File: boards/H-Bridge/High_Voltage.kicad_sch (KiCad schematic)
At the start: 3 parts, among them IC2 MIC4606-1YML-TR, IC3 AD8410AWBRZ-RL

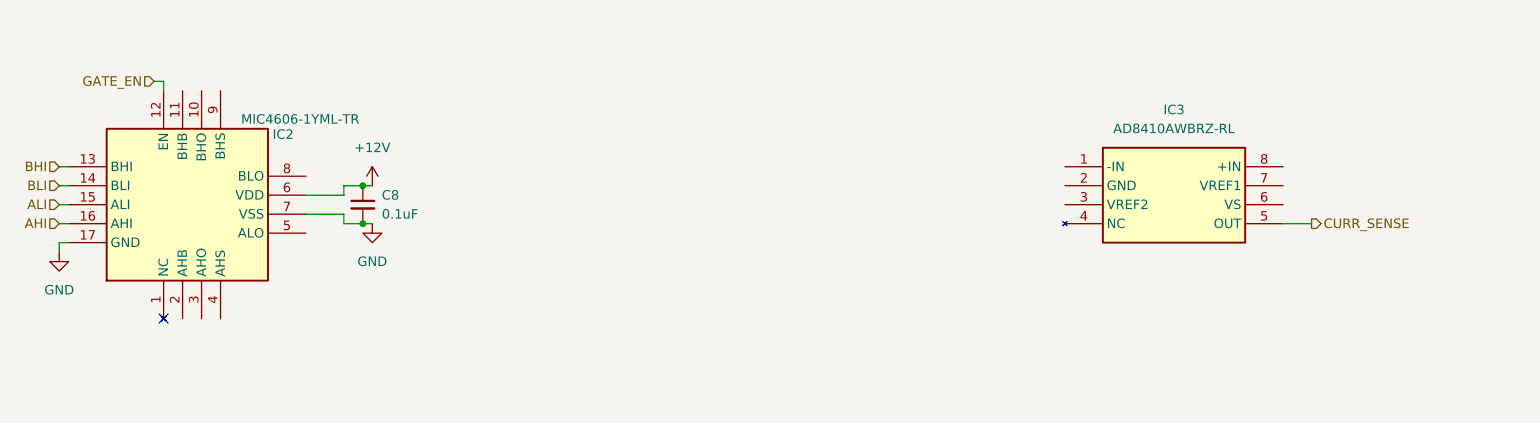
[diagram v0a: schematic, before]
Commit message: Added symbols + fixed sheet layout, low voltage nearly complete
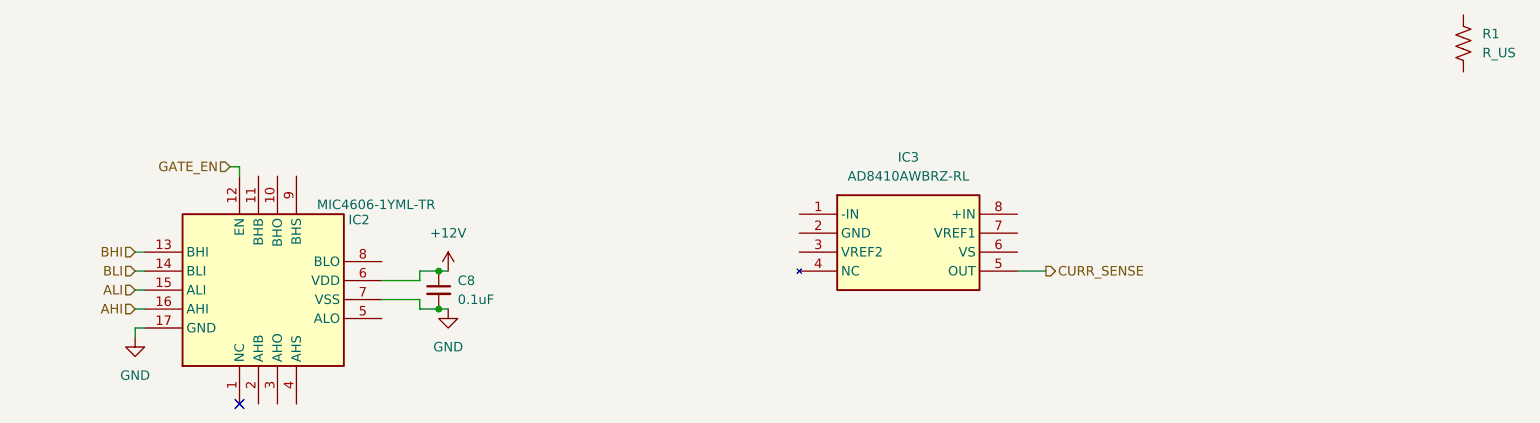
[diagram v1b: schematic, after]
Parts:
- added R1: R_US, symbol Device:R_US
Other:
- moved on the sheet: C8, IC2, IC3

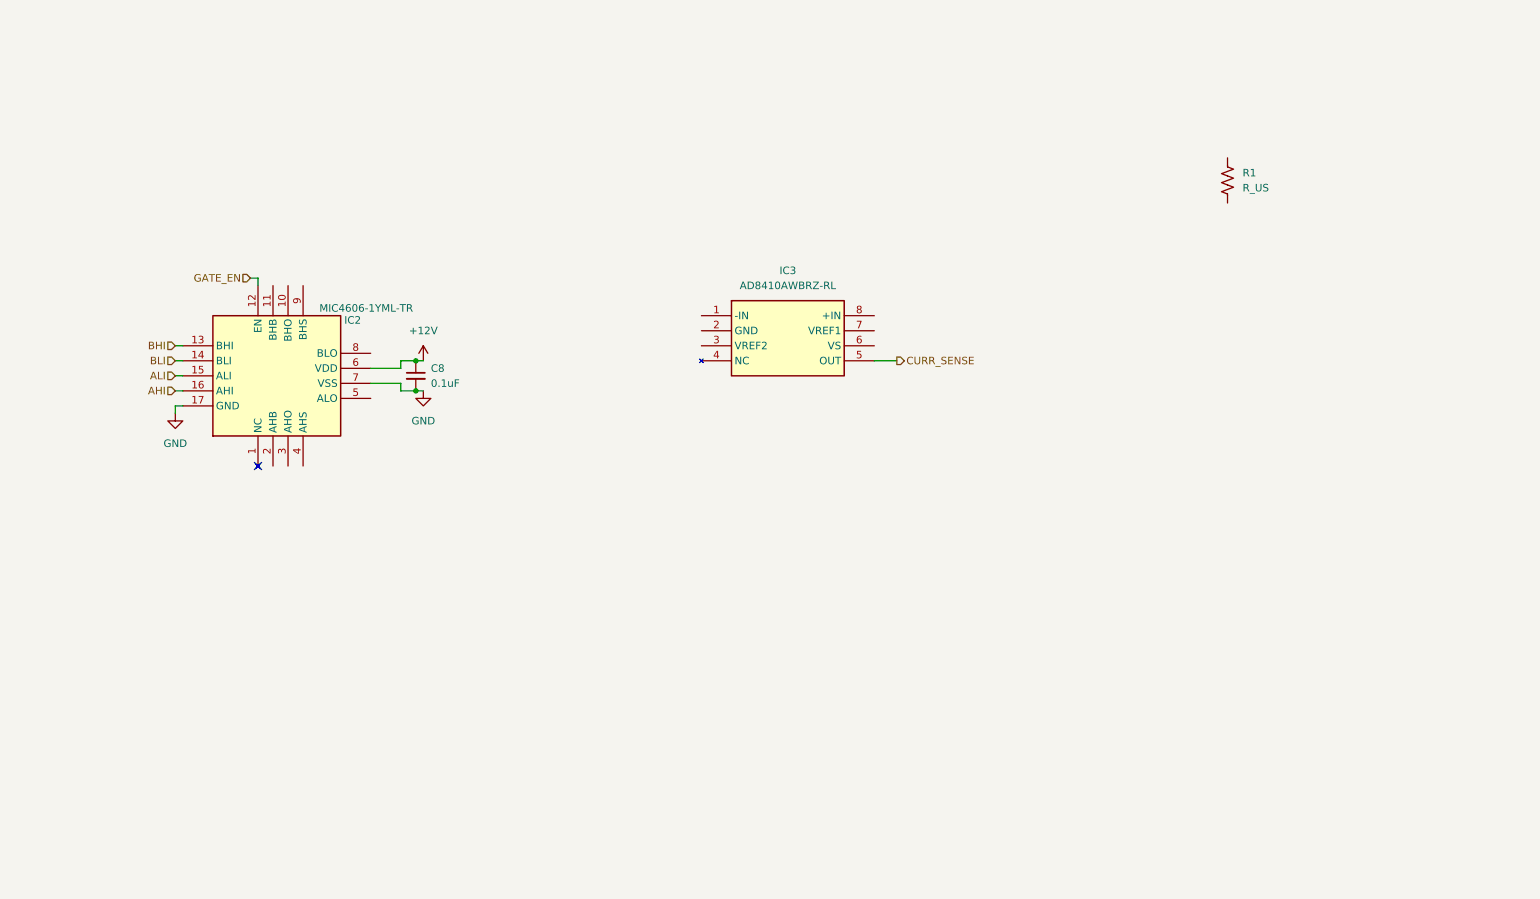
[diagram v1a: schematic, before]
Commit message: added fet sym,  hv schematic changes
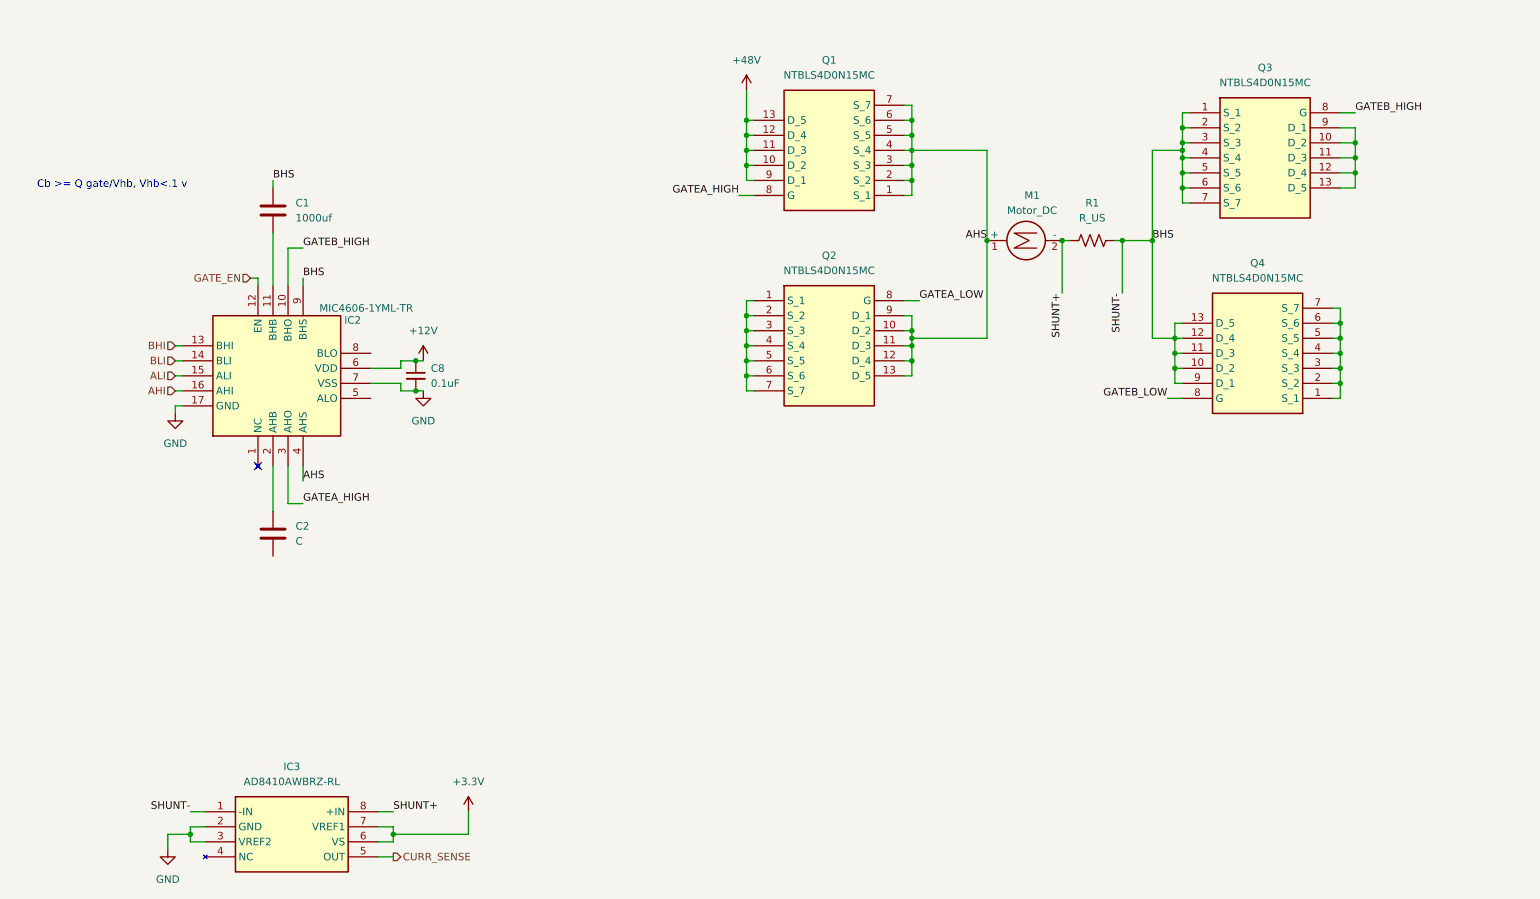
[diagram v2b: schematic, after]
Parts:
- added C1: 1000uf, symbol Device:C
- added C2: C, symbol Device:C
- added M1: Motor_DC, symbol Motor:Motor_DC
- added Q1, Q2, Q3, Q4: NTBLS4D0N15MC, High Power MOSFETs:NTBLS4D0N15MC, symbol High Power MOSFETs:NTBLS4D0N15MC
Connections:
- net GND: now also IC3.2 (GND), IC3.3 (VREF2)
- net BHS: now reaches IC3.1 (-IN)
- net BHS: now also IC2.9 (BHS), R1.2, C1.1, Q3.1 (S_1), Q3.2 (S_2), Q3.3 (S_3), Q3.4 (S_4), Q3.5 (S_5), Q3.6 (S_6), Q3.7 (S_7), Q4.10 (D_2), Q4.11 (D_3), Q4.12 (D_4), Q4.13 (D_5), Q4.9 (D_1)
- net +3.3V: now reaches IC3.6 (VS)
- net +3.3V: now also IC3.7 (VREF1)
- net SHUNT+: now reaches IC3.8 (+IN)
- net SHUNT+: now also R1.1, M1.2 (-)
- net GATEB_HIGH: now reaches IC2.10 (BHO)
- net GATEB_HIGH: now also Q3.8 (G)
- net at IC2.11 (BHB): now also C1.2
- net at IC2.2 (AHB): now also C2.1
- net GATEA_HIGH: now reaches IC2.3 (AHO)
- net GATEA_HIGH: now also Q1.8 (G)
- net AHS: now reaches IC2.4 (AHS)
- net AHS: now also M1.1 (+), Q1.1 (S_1), Q1.2 (S_2), Q1.3 (S_3), Q1.4 (S_4), Q1.5 (S_5), Q1.6 (S_6), Q1.7 (S_7), Q2.10 (D_2), Q2.11 (D_3), Q2.12 (D_4), Q2.13 (D_5), Q2.9 (D_1)
- new net: Q2.1 (S_1), Q2.2 (S_2), Q2.3 (S_3), Q2.4 (S_4), Q2.5 (S_5), Q2.6 (S_6), Q2.7 (S_7)
- new net: Q4.1 (S_1), Q4.2 (S_2), Q4.3 (S_3), Q4.4 (S_4), Q4.5 (S_5), Q4.6 (S_6), Q4.7 (S_7)
- new net: Q3.10 (D_2), Q3.11 (D_3), Q3.12 (D_4), Q3.13 (D_5), Q3.9 (D_1)
- new net +48V: Q1.10 (D_2), Q1.11 (D_3), Q1.12 (D_4), Q1.13 (D_5), Q1.9 (D_1)
- new net GATEA_LOW: Q2.8 (G)
- new net GATEB_LOW: Q4.8 (G)
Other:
- note added: "Cb >= Q gate/Vhb, Vhb<.1 v"
- moved on the sheet: IC3, R1

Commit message: finished schematic (i think), added footprints
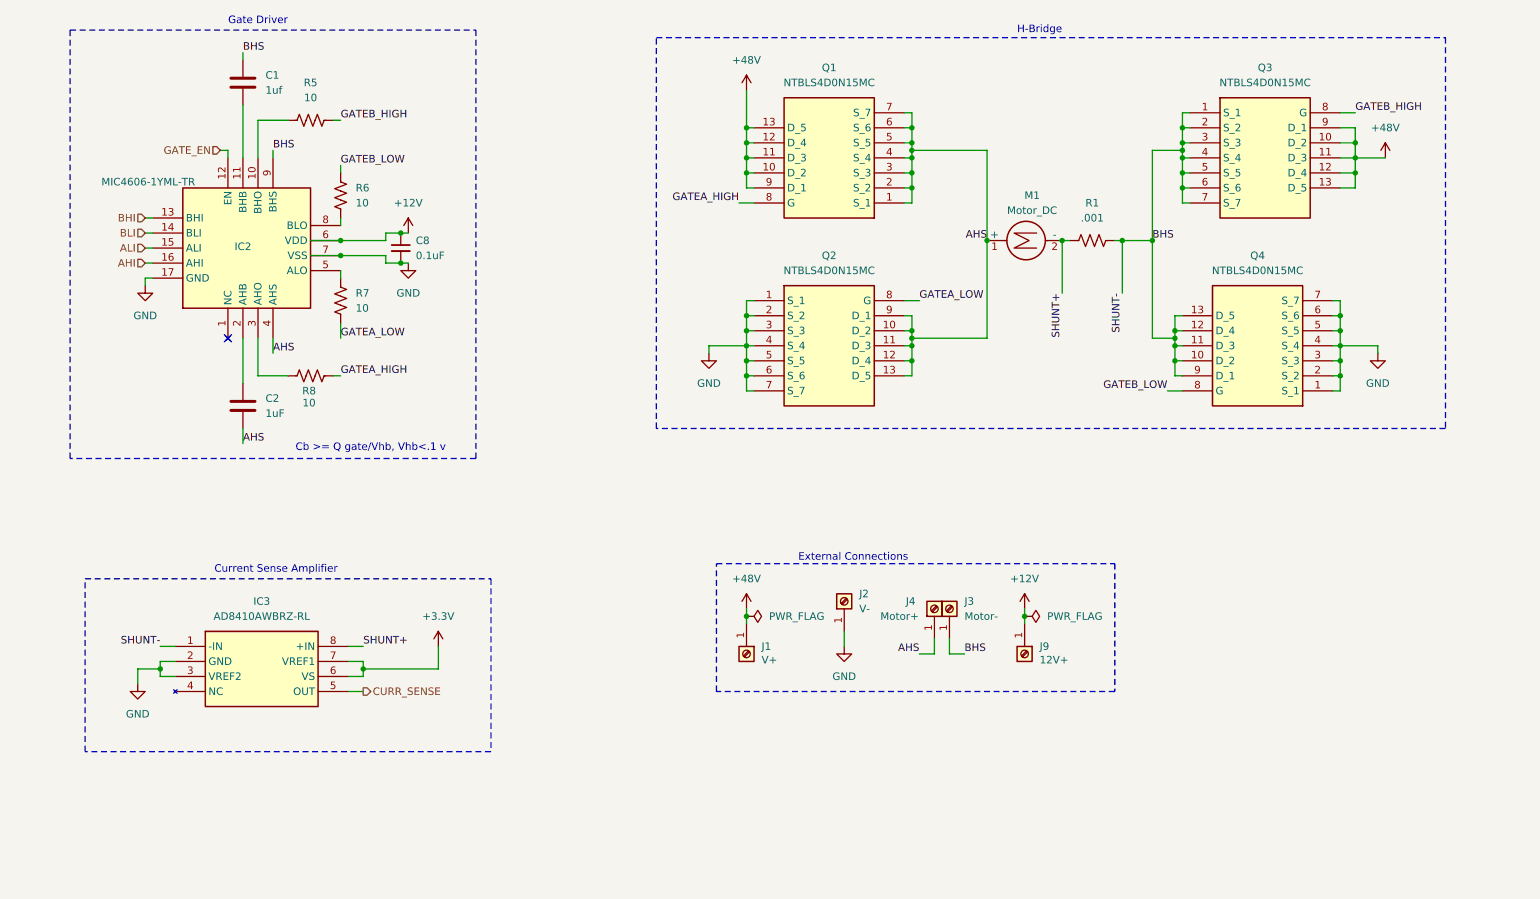
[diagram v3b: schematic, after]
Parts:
- added J1: V+, ThreadedConnector:WP-BUTR_7460307, symbol Connector:Screw_Terminal_01x01
- added J2: V-, ThreadedConnector:WP-BUTR_7460307, symbol Connector:Screw_Terminal_01x01
- added J3: Motor-, ThreadedConnector:WP-BUTR_7460307, symbol Connector:Screw_Terminal_01x01
- added J4: Motor+, ThreadedConnector:WP-BUTR_7460307, symbol Connector:Screw_Terminal_01x01
- added J9: 12V+, ThreadedConnector:WP-BUTR_7460307, symbol Connector:Screw_Terminal_01x01
- added R5, R6, R7, R8: 10, symbol Device:R_US
- C1: value 1000uf -> 1uf
- C2: value C -> 1uF
- R1: value R_US -> .001; footprint (none) -> Resistor_SMD:R_2512_6332Metric
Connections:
- net +12V: now also J9.1 (Pin_1)
- net +48V: now also Q3.10 (D_2), Q3.11 (D_3), Q3.12 (D_4), Q3.13 (D_5), Q3.9 (D_1), J1.1 (Pin_1)
- net AHS: now also C2.2, J4.1 (Pin_1)
- net BHS: now also J3.1 (Pin_1)
- net GATEA_HIGH: now also R8.2; no longer IC2.3 (AHO)
- net GATEA_LOW: now also R7.1
- net GATEB_HIGH: now also R5.2; no longer IC2.10 (BHO)
- net GATEB_LOW: now also R6.2
- net GND: now also Q2.1 (S_1), Q2.2 (S_2), Q2.3 (S_3), Q2.4 (S_4), Q2.5 (S_5), Q2.6 (S_6), Q2.7 (S_7), Q4.1 (S_1), Q4.2 (S_2), Q4.3 (S_3), Q4.4 (S_4), Q4.5 (S_5), Q4.6 (S_6), Q4.7 (S_7), J2.1 (Pin_1)
- net at IC2.5 (ALO): now also R7.2
- net at IC2.8 (BLO): now also R6.1
- new net: IC2.3 (AHO), R8.1
- new net: IC2.10 (BHO), R5.1
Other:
- note added: "Current Sense Amplifier"
- note added: "External Connections"
- note added: "Gate Driver"
- note added: "H-Bridge"
- moved on the sheet: C1, C2, C8, IC2, IC3, Q1, Q4

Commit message: added bulk caps to h bridge
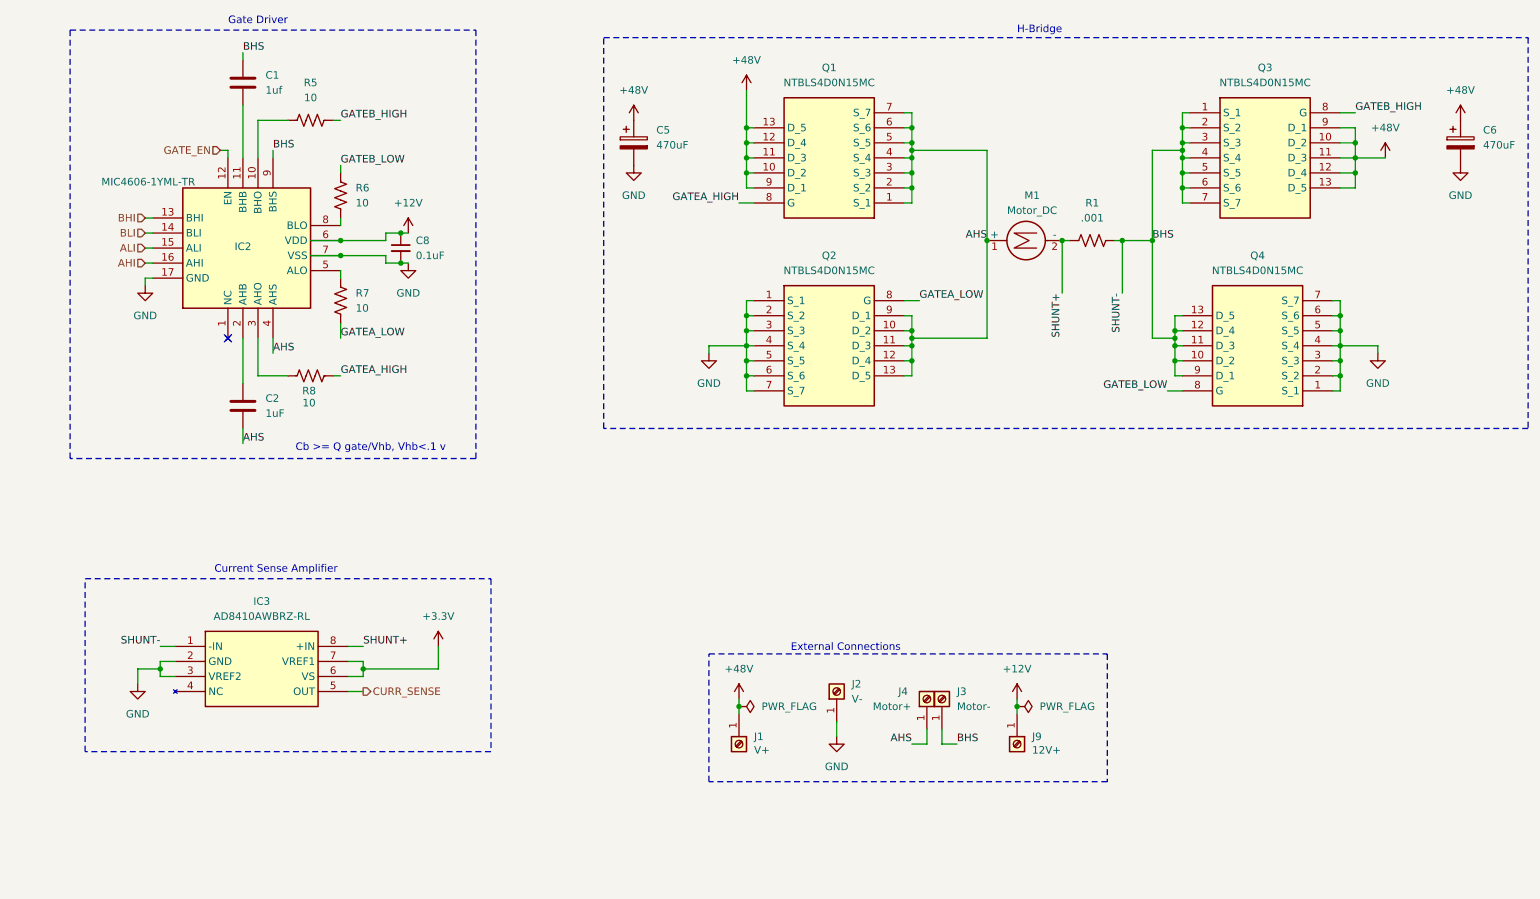
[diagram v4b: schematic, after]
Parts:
- added C5, C6: 470uF, symbol Device:C_Polarized
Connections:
- net +48V: now also C5.1, C6.1
- net GND: now also C5.2, C6.2
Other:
- moved on the sheet: J1, J2, J3, J4, J9

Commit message: finished schematic, added footprint assignments
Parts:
- C1, C2: footprint (none) -> Capacitor_SMD:C_0603_1608Metric
- C5, C6: footprint (none) -> Capacitor_THT:CP_Radial_D10.0mm_P7.50mm
- C8: footprint (none) -> Capacitor_SMD:C_0402_1005Metric
- IC2: footprint QFN65P400X400X90-17N-D -> Package_DFN_QFN:QFN-16-1EP_4x4mm_P0.65mm_EP2.5x2.5mm
- IC3: footprint SOIC127P600X175-8N -> Package_SO:MSOP-8_3x3mm_P0.65mm
- R5, R6, R7, R8: footprint (none) -> Resistor_SMD:R_0603_1608Metric
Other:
- moved on the sheet: IC3, J1, J2, J3, J4, J9

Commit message: did some layout
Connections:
- net AHS: now also IC3.8 (+IN), R1.1; no longer J4.1 (Pin_1), M1.1 (+)
- net BHS: now also M1.2 (-); no longer IC3.1 (-IN), R1.2
- removed net SHUNT+: IC3.8 (+IN), M1.2 (-), R1.1
- new net SHUNT-: IC3.1 (-IN), J4.1 (Pin_1), M1.1 (+), R1.2
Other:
- moved on the sheet: M1, R1
